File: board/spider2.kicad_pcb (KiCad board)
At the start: 2 copper layers, 137 x 72.5 mm, 121 parts, among them J1 NRJ6HH, J10 PJ-320A, J11 PJ359, J12 PJ359, J13 PJ359, J14 PJ359, J15 PJ359, J16 PJ359, J19 PJ359, J2 NRJ6HH, J20 PJ359, J3 PJ359, J4 PJ359, J5 PJ359, J6 PJ-320A, J7 PJ359, J8 PJ359, J9 PJ359, P1 USB4085, Q1 AOI4286, Q2 BC547, Q3 BC547, SW4 200MDP3T1B1M6QE, U2 AP63203, U4 NE5532, U5 MAX4062, U6 MAX4062, U7 PAM8406D

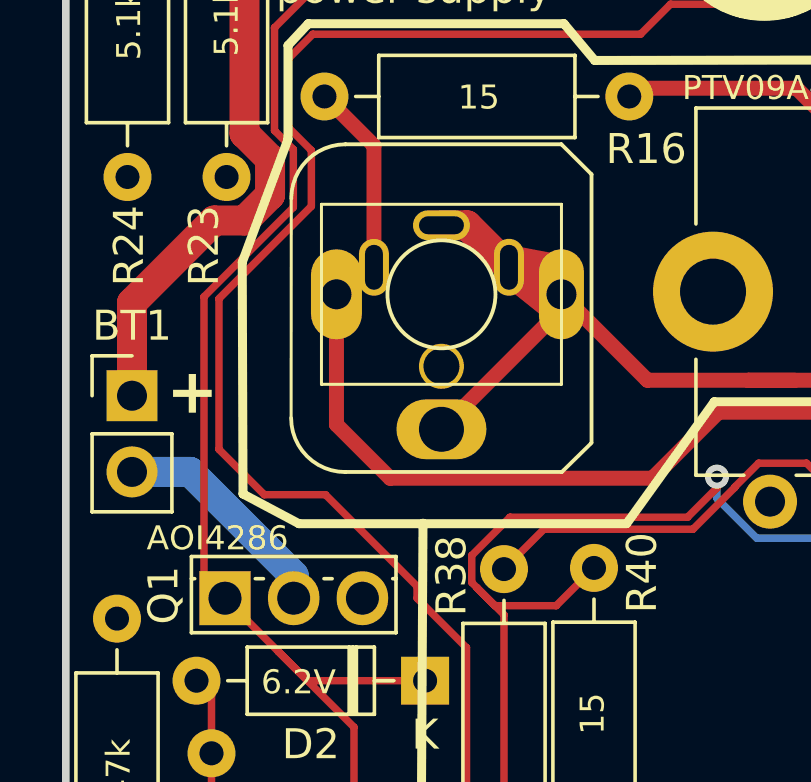
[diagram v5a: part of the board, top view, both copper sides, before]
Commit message: slot for cable tieing the battery cable
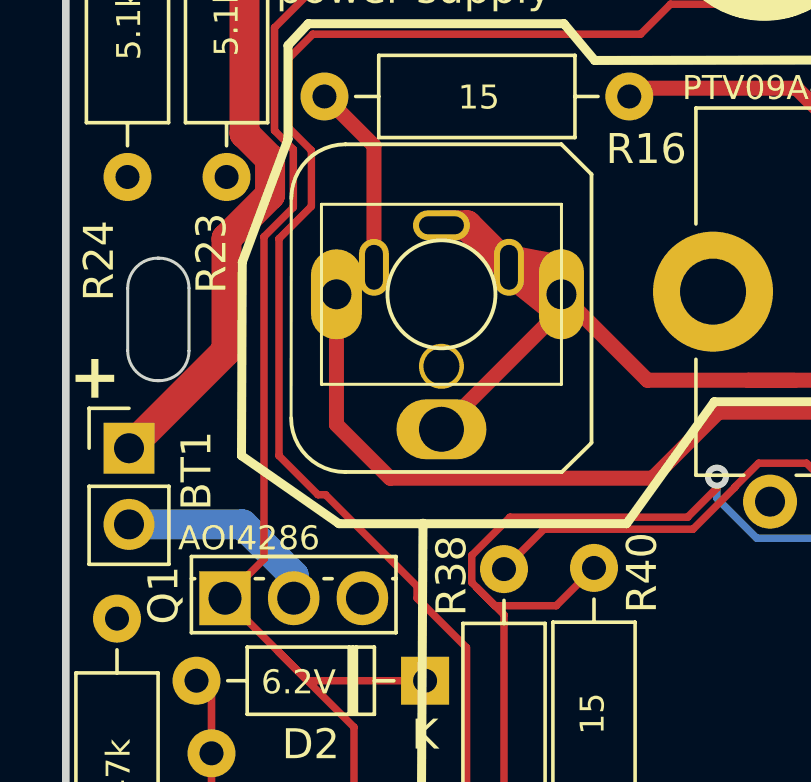
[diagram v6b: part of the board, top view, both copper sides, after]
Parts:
- moved BT1 1.75 mm to (139.8, 62.0)
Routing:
- net +3.3V: track 256.9 -> 254.2 mm
- net Net-(BT1-+): track 22.8 -> 24.0 mm
- net Net-(BT1--): track 7.58 -> 6.95 mm
- net +BATT: track 71.8 -> 71.3 mm
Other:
- outline, holes or cut-outs redrawn

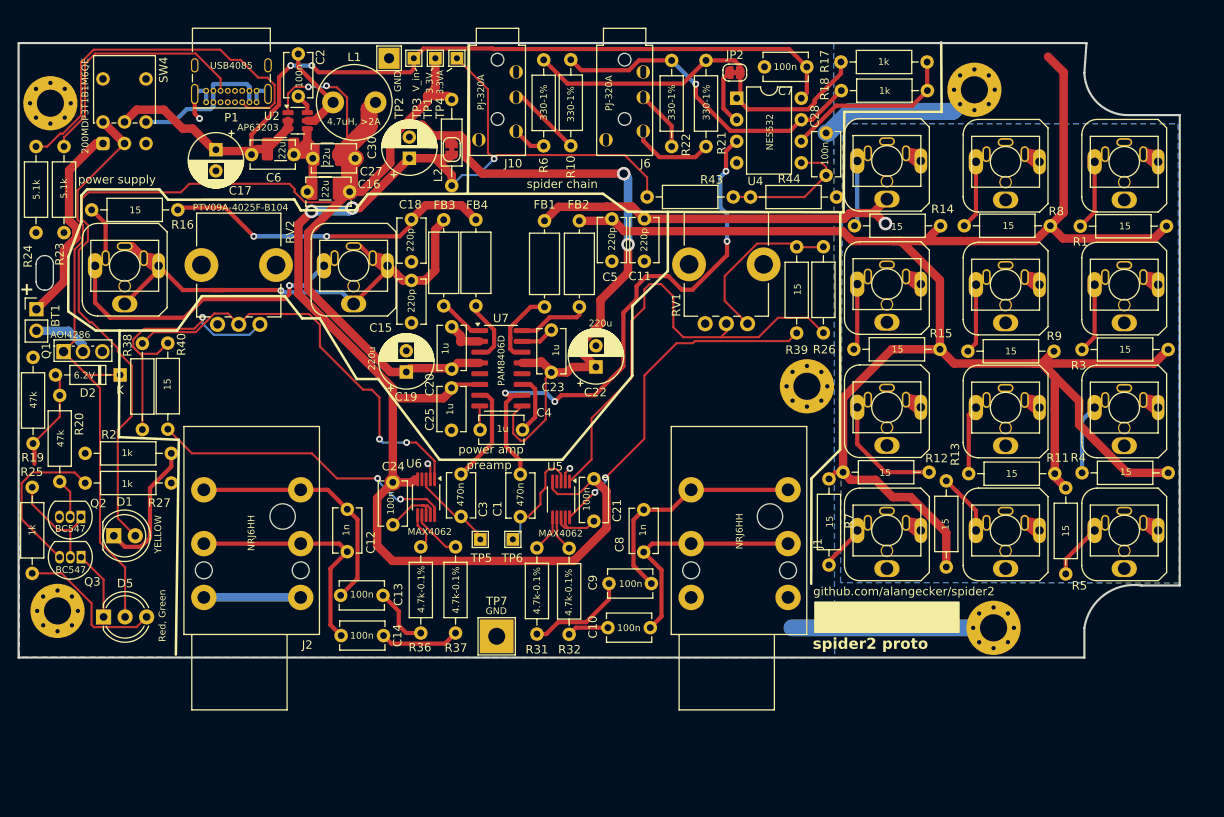
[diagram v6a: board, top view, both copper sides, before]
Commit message: bypass capacitor footprints smaller and closer
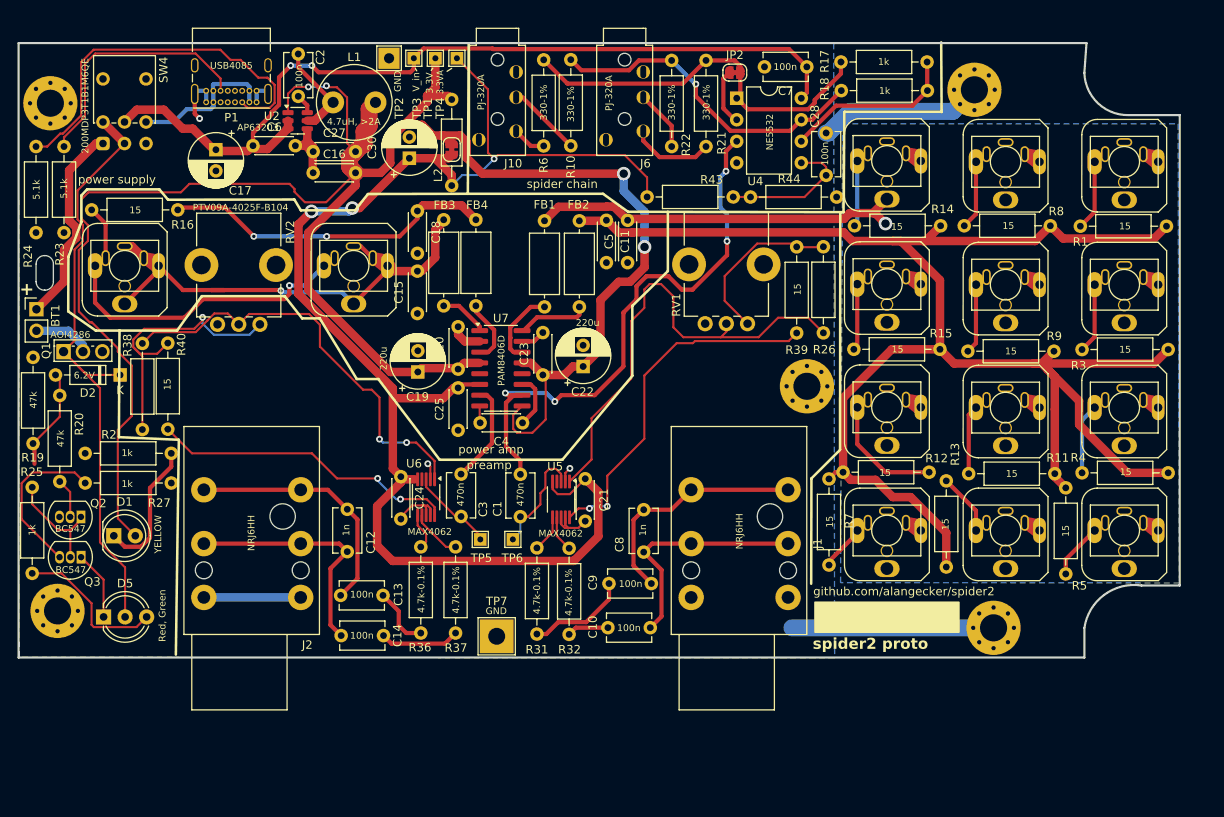
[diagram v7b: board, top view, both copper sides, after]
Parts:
- removed C33, C35, C36: alt, Capacitor_SMD:C_1210_3225Metric_Pad1.33x2.70mm_HandSolder
- C11, C15, C16, C18, C20, C21, C23, C24, C25, C27, C4, C5, C6: footprint Capacitor_THT:C_Disc_D5.1mm_W3.2mm_P5.00mm -> Capacitor_THT:C_Disc_D4.3mm_W1.9mm_P5.00mm
- moved C16 2.34 mm to (172.4, 45.9)
- moved C5 1.99 mm to (209.5, 56.5)
- moved C22 1.52 mm to (204.2, 68.8)
- moved C19 1.36 mm to (184.8, 69.4)
- moved C15 1.30 mm to (184.7, 62.5)
- moved C18 1.22 mm to (184.7, 50.4)
- moved C24 1.17 mm to (182.8, 81.8)
- moved C6 1.06 mm to (165.3, 42.7)
- moved C23 1.04 mm to (199.5, 69.8)
- moved C21 1.03 mm to (204.5, 82.0)
- moved C4 0.82 mm to (197.1, 75.4)
- moved C27 0.80 mm to (172.4, 43.4)
- moved C25 0.78 mm to (189.5, 76.3)
- moved C20 0.75 mm to (189.5, 69.1)
- moved C11 0.67 mm to (207.0, 51.5)
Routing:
- net Net-(C11-Pad1): track 224.1 -> 202.6 mm
- net GND: track 111.7 -> 103.2 mm
- net Net-(C15-Pad2): track 61.7 -> 57.6 mm
- net +3.3V: track 254.2 -> 251.7 mm
- net Net-(U5-G1): track 40.5 -> 42.3 mm
- net +3.3VA: track 166.7 -> 165.0 mm
- net VCC: track 104.7 -> 103.6 mm
- net Net-(U7-VREF): track 2.84 -> 2.01 mm

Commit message: multiple changes
- correct transistor footprints
- swap led green/red
- PAM input resistor
- poti adjustments
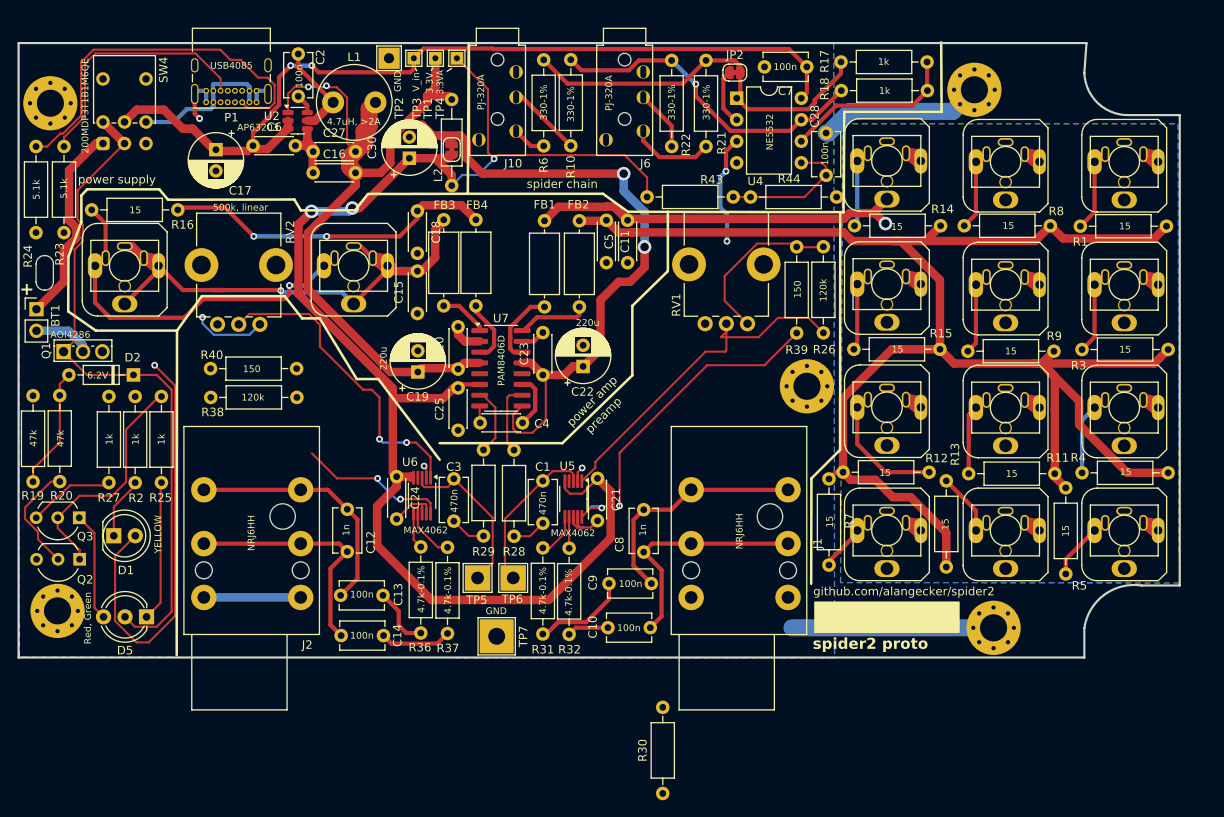
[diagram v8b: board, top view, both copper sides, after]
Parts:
- added R28: 270k, Resistor_THT:R_Axial_DIN0207_L6.3mm_D2.5mm_P10.16mm_Horizontal, F.Cu at (196.1, 88.8)
- added R29: 270k, Resistor_THT:R_Axial_DIN0207_L6.3mm_D2.5mm_P10.16mm_Horizontal, F.Cu at (192.5, 88.8)
- added R30: 1k, Resistor_THT:R_Axial_DIN0207_L6.3mm_D2.5mm_P10.16mm_Horizontal, F.Cu at (213.7, 119.1)
- Q2, Q3: footprint Package_TO_SOT_THT:TO-92_Inline -> Package_TO_SOT_THT:TO-92_Inline_Wide
- R26, R38: value NC -> 120k
- R39, R40: value 15 -> 150
- RV1, RV2: value PTV09A-4025F-B104 -> 500k, linear
- TP5, TP6: footprint TestPoint:TestPoint_THTPad_1.5x1.5mm_Drill0.7mm -> TestPoint:TestPoint_THTPad_3.0x3.0mm_Drill1.5mm
- moved R25 18.6 mm to (154.5, 82.5)
- moved R38 18.6 mm to (170.5, 72.4), turned to 180 degrees
- moved R40 16.8 mm to (170.4, 69.0), turned to 180 degrees
- moved R2 8.93 mm to (151.4, 72.3), turned to -90 degrees
- moved D5 5.07 mm to (152.7, 98.3), turned to 180 degrees
- moved Q2 5.00 mm to (144.8, 91.5)
- moved C1 4.99 mm to (199.5, 82.2), turned to -90 degrees
- moved Q3 4.66 mm to (144.8, 86.6)
- moved TP5 4.55 mm to (191.8, 93.7)
- moved TP6 4.55 mm to (196.0, 93.7)
- moved C3 4.53 mm to (189.0, 82.0), turned to -90 degrees
- moved R19 4.52 mm to (139.3, 82.4)
- moved R27 2.80 mm to (148.3, 82.5), turned to 90 degrees
- moved D2 1.58 mm to (151.2, 69.8)
- moved C21 1.45 mm to (205.9, 81.9)
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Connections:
- C1 pad 1: /Preamp Interpreter/OUT -> INT_OUT
- C1 pad 2: INT_OUT -> Net-(C1-Pad2)
- C3 pad 2: Net-(U7-INL) -> Net-(C3-Pad2)
- Q3 pad 1: Net-(D5-K1) -> Net-(D5-K2)
- R25 pad 1: Net-(D5-K2) -> Net-(D5-K1)
- TP6 pad 1: /Preamp Interpreter/OUT -> INT_OUT
- U4 pad 3: INT_OUT -> Net-(U4A-+)
- U5 pad 3: /Preamp Interpreter/OUT -> INT_OUT
- U7 pad 10: INT_OUT -> Net-(U7-INR)
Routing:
- net INT_OUT: track 67.8 -> 18.8 mm, vias 4 -> 0
- net +3.3V: track 251.7 -> 222.4 mm, vias 4 -> 5
- net Net-(R38-Pad1): track 33.8 -> 8.55 mm
- net Net-(U6-G1): track 36.4 -> 17.8 mm
- net Net-(Q2-C): track 13.1 -> 27.8 mm
- net Net-(U6-G2): track 50.7 -> 37.0 mm
- net Net-(U5-G2): track 56.0 -> 42.6 mm
- net /Preamp Interpreter/OUT: track 13.2 -> 0.00 mm
- net Net-(U4A-+): track 0.00 -> 13.0 mm, vias 0 -> 2
- net /Preamp Floor/OUT: track 10.1 -> 19.7 mm
- net Net-(D1-K): track 16.3 -> 7.31 mm
- net Net-(Q3-E): track 19.1 -> 10.3 mm
- net Net-(D5-K1): track 8.15 -> 16.6 mm
- net Net-(U7-INR): track 0.00 -> 8.41 mm
- net Net-(Q2-B): track 4.68 -> 13.1 mm
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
